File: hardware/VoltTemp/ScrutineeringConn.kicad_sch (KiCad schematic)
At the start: 3 parts, among them J1 ScrutineeringConn

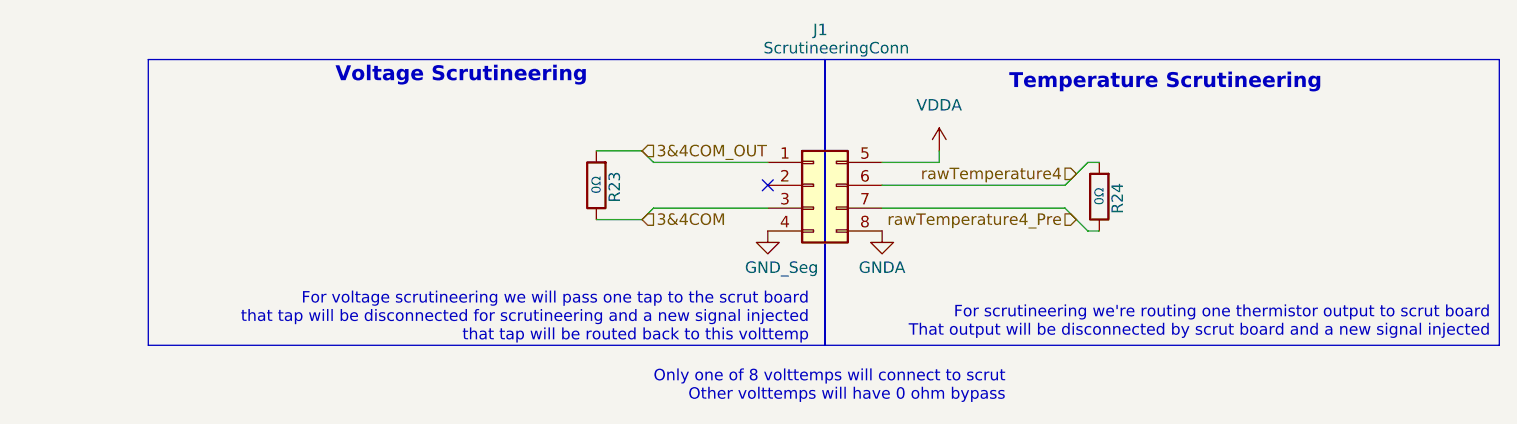
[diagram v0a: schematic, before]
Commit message: Boot switch changed to V_Boot, ShieldGND added to scrut conn, labels added to LEDs, misc routing tweaks
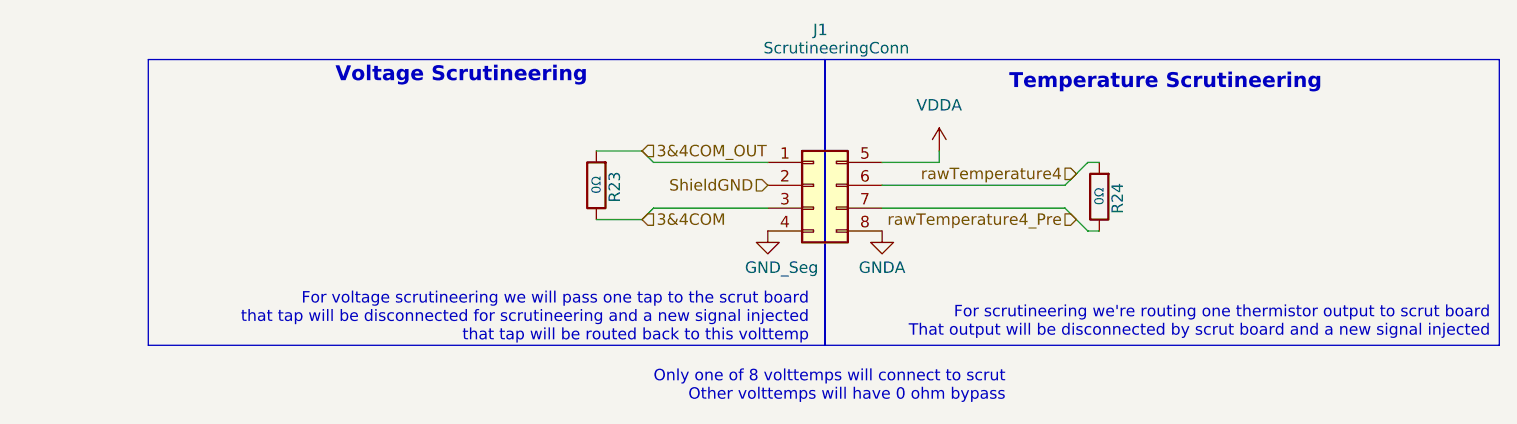
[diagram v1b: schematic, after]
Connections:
- net ShieldGND: now reaches J1.2 (Pin_2)
- no-connect marks 1 -> 0
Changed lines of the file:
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@@
 		)
-	)
-	(no_connect
-		(at 85.09 57.15)
 	)
 	(wire
@@
 		)
 	)
+	(hierarchical_label "ShieldGND"
+		(shape input)
+		(at 85.09 57.15 180)
+		(effects
+			(font
+				(size 1.27 1.27)
+			)
+			(justify right)
+		)
+	)
